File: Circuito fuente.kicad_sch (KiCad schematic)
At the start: 38 parts, among them Q1 TIP122, U1 Bornera_1x3, U2 Bornera_1x2, U24 Trafo: 15+15, U3 Bornera_1x3, U35 LM7812_TO220, U39 LM7912_TO220, U4 LM7812_TO220, U40 LM7805_TO220, U41 LM7905_TO220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

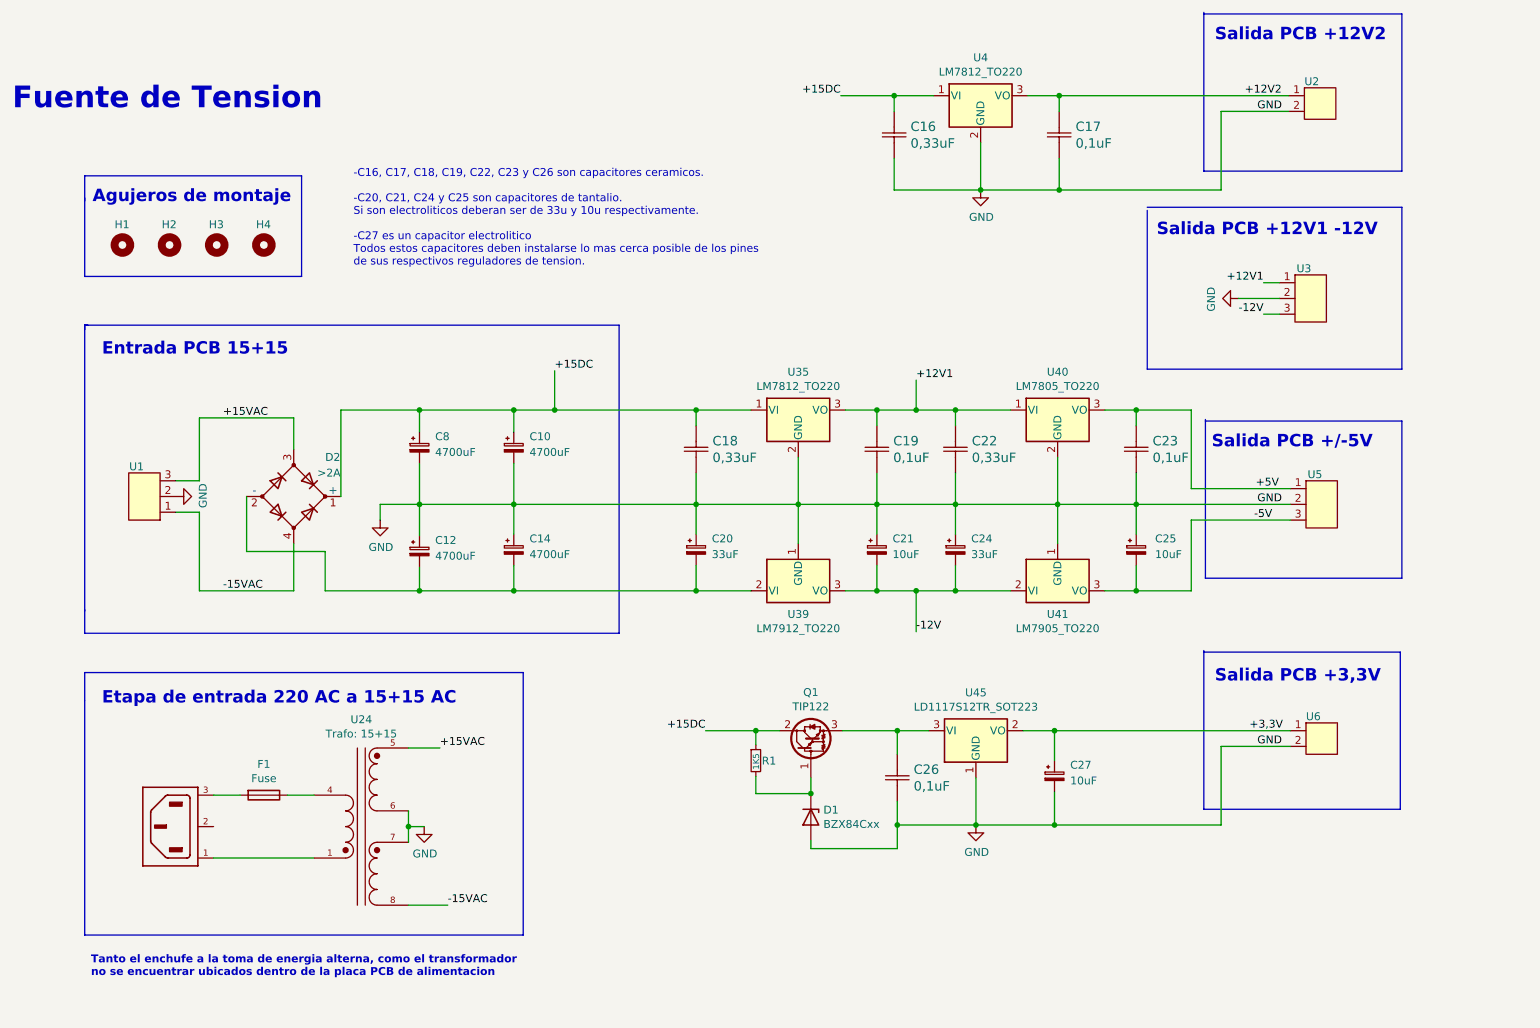
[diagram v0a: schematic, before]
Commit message: Reordering schematic
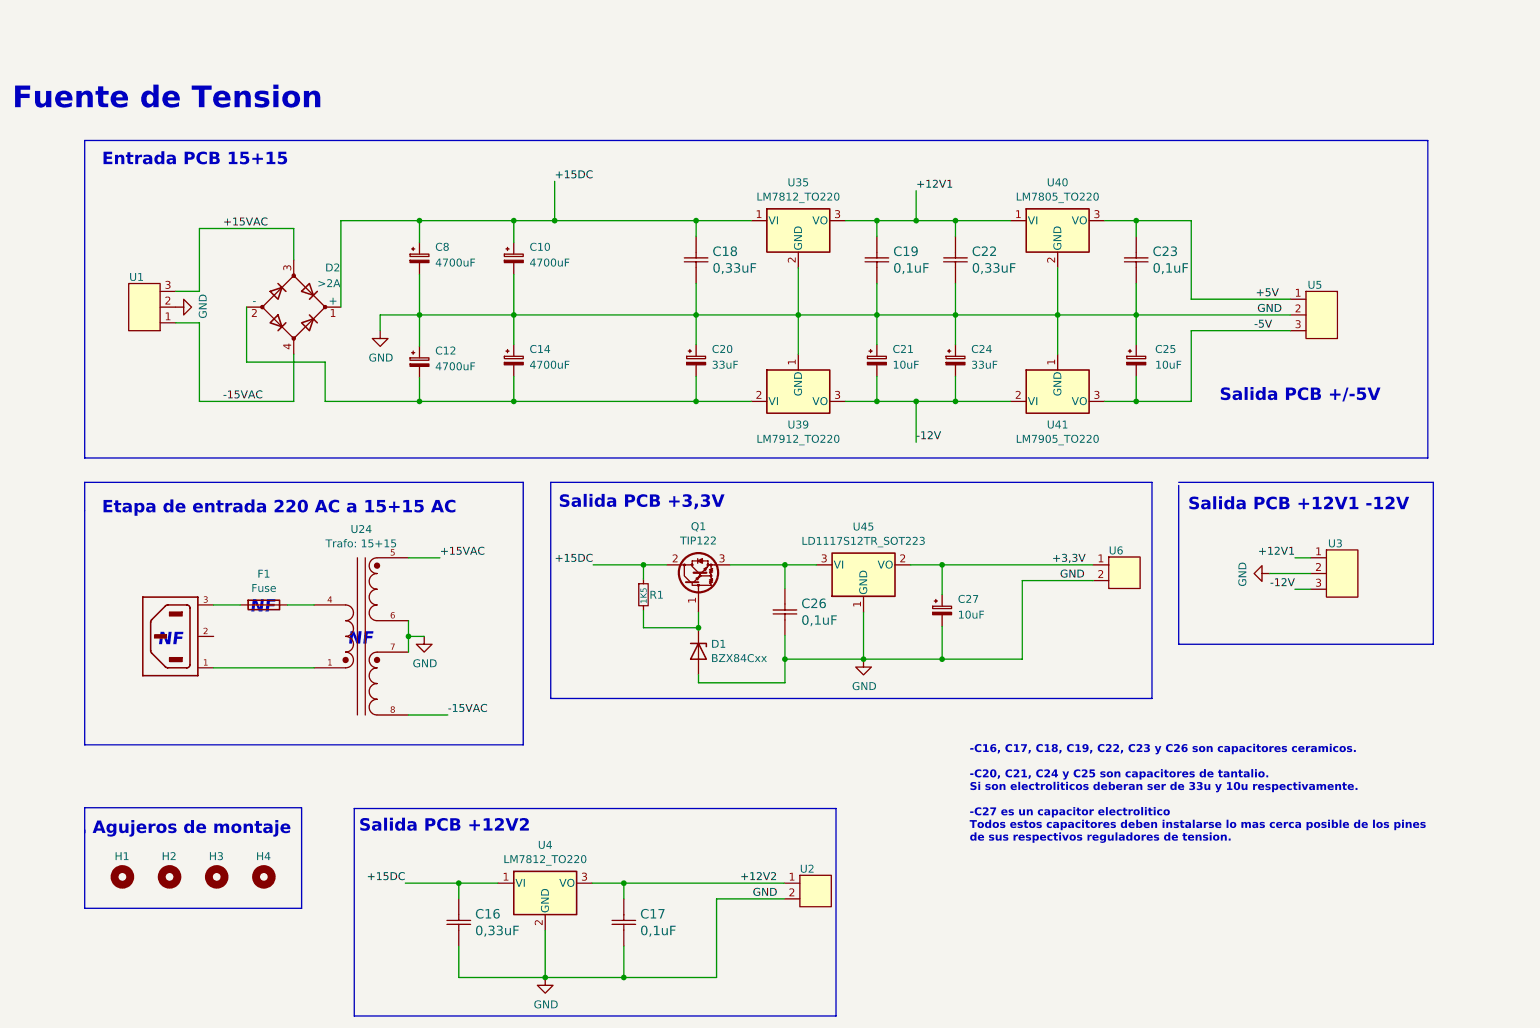
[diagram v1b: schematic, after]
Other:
- note added: "NF"
- note removed: "Tanto el enchufe a la toma de energia alterna, como el transformador no se encuentrar ubicados dentro de la placa PCB de alimentacion"
- moved on the sheet: C10, C12, C14, C16, C17, C18, C19, C20, C21, C22, C23, C24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
